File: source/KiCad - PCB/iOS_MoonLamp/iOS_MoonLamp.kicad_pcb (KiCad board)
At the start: 2 copper layers, 60 x 60 mm, 34 parts, among them J1 USB_C_Receptacle_USB2.0_16P, SW1 (BOOT), SW2 (EN), SW3 (CTRL), U1 AMS1117-3.3, U2 CP2102N-Axx-xQFN28, U3 ESP32-WROOM-32, U4 PC817

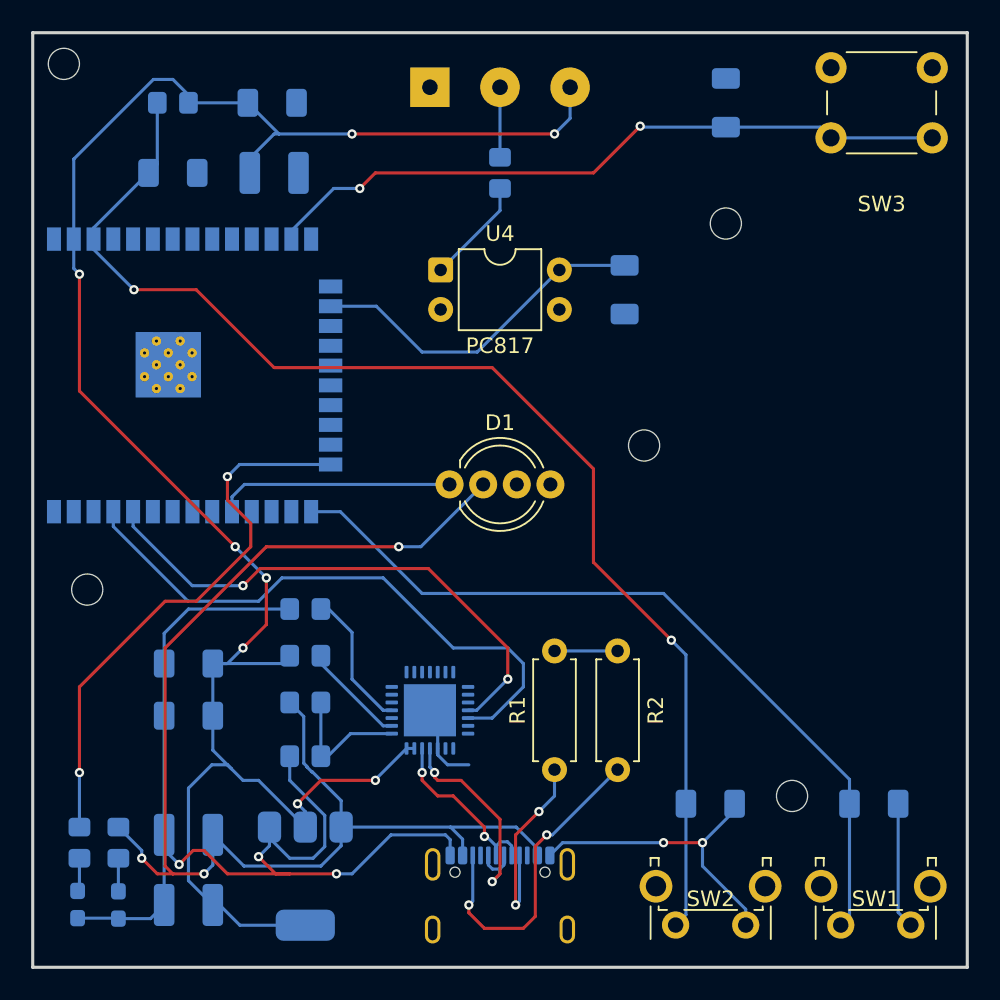
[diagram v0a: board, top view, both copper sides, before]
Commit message: Rerouted the PCB
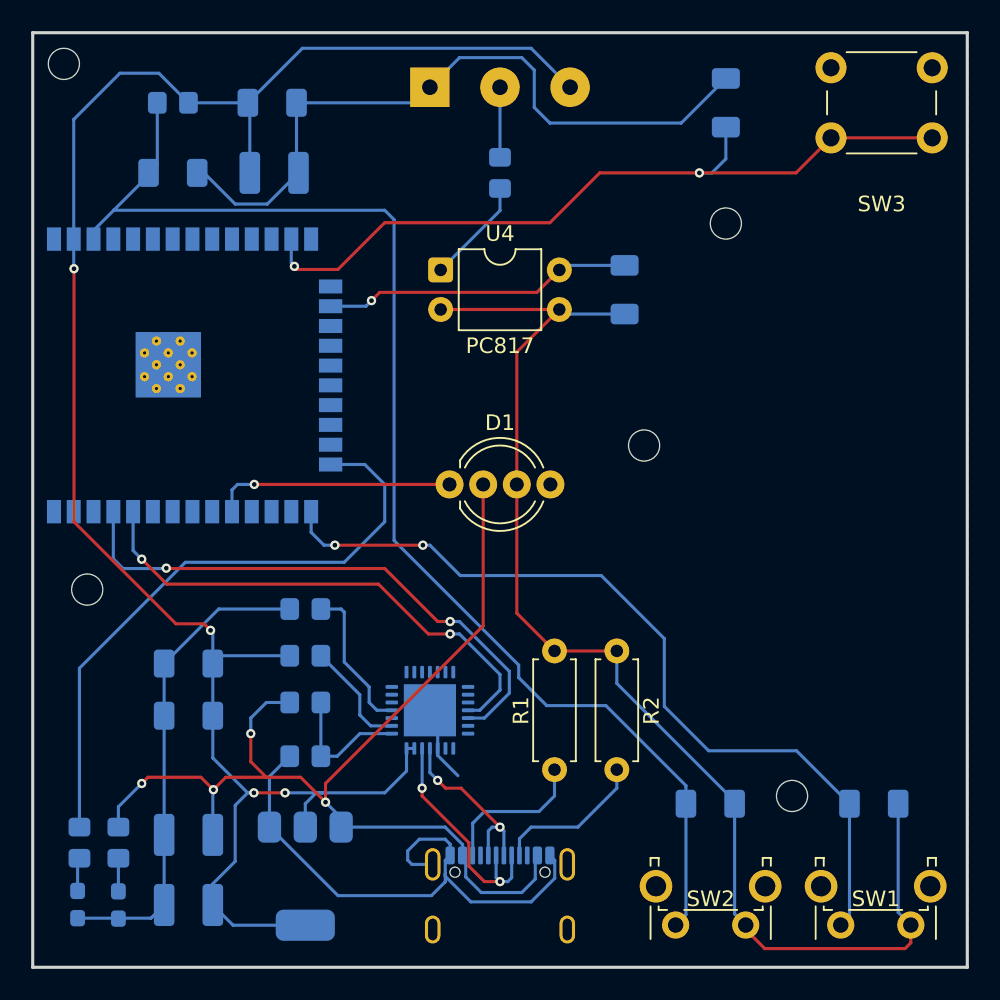
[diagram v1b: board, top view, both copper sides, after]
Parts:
- moved R2 4.05 mm to (153.5, 118.3)
- moved R1 4.00 mm to (157.5, 118.3)
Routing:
- net GND: track 108.9 -> 200.2 mm, vias 5 -> 0
- net 5V: track 85.2 -> 70.6 mm, vias 3 -> 4
- net Net-(J1-CC2): track 20.6 -> 9.73 mm, vias 2 -> 0
- net IO14: track 44.8 -> 50.5 mm
- net IO2: track 35.8 -> 40.1 mm, vias 2 -> 0
- net D-: track 11.3 -> 15.3 mm
- net 3V: track 128.6 -> 125.2 mm, vias 8 -> 4
- net EN: track 81.1 -> 84.2 mm, vias 2 -> 0
- net Net-(J1-CC1): track 13.0 -> 9.86 mm, vias 2 -> 0
- net D+: track 14.9 -> 11.8 mm
- net IO13: track 22.4 -> 20.0 mm, vias 0 -> 1
- net IO0: track 51.3 -> 53.7 mm, vias 0 -> 2
- net TXD: track 38.0 -> 36.2 mm, vias 0 -> 2
- net RXD: track 34.5 -> 32.9 mm
- net Net-(U2-~{SUSPEND}): track 9.00 -> 9.70 mm
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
